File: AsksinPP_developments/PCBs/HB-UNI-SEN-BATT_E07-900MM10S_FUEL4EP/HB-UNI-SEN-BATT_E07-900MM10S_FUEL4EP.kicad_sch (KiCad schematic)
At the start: 32 parts, among them J1 Conn_01x02, J10 charge, J11 ePaper connector, J12 U.FL connector, J2 Conn_01x02, J3 Conn_01x02, J4 Conn_01x02, J5 ISP Programmer, J6 Conn_01x04, J7 Conn_01x04, J8 Conn_01x04, J9 Conn_01x04, Q1 IRLU024N, SW1 config button

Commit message: PCBs: added HB-UNI-SEN-BATT_ATMega1284P_E07-900MM10S_FUEL4EP; fies fixes for HB-UNI-SEN-BATT_ATMega1284P_E07-868MS10_FUEL4EP and HB-UNI-SEN-BATT_E07-900MM10S_FUEL4EP
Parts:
- Module1: footprint U.FL connector (optional) -> FUEL4EP:eByte_E07-900MM10S
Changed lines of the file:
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@@
       (effects (font (size 1.27 1.27) bold))
     )
-    (property "Footprint" "U.FL connector (optional)" (id 2) (at 90.17 181.61 0)
+    (property "Footprint" "FUEL4EP:eByte_E07-900MM10S" (id 2) (at 90.17 181.61 0)
       (effects (font (size 1.27 1.27)) hide)
     )
@@
     )
     (path "/355609ac-841a-4e6b-bbeb-2d1eb180bf65"
-      (reference "Module1") (unit 1) (value "E07-900MM10S") (footprint "U.FL connector (optional)")
+      (reference "Module1") (unit 1) (value "E07-900MM10S") (footprint "FUEL4EP:eByte_E07-900MM10S")
     )
     (path "/00000000-0000-0000-0000-0000615b04ce"

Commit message: PCBs/HB-UNI-SEN-BATT_E07-900MM10S_FUEL4EP: migration to KiCAD 8
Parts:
- removed J12: U.FL connector, FUEL4EP:U.FL_Molex_MCRF_73412-0110_Vertical, symbol Connector:Conn_Coaxial_x2_Isolated
- added J12: U.FL connector, FUEL4EP:U.FL_Molex_MCRF_73412-0110_Vertical, symbol Connector:Conn_Coaxial
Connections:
- net GND: now also J12.2 (Ext)
- net at AE1.1 (A), Module1.1B (ANT): now also J12.1 (In)
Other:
- moved on the sheet: D1, Module2, R1, SW1

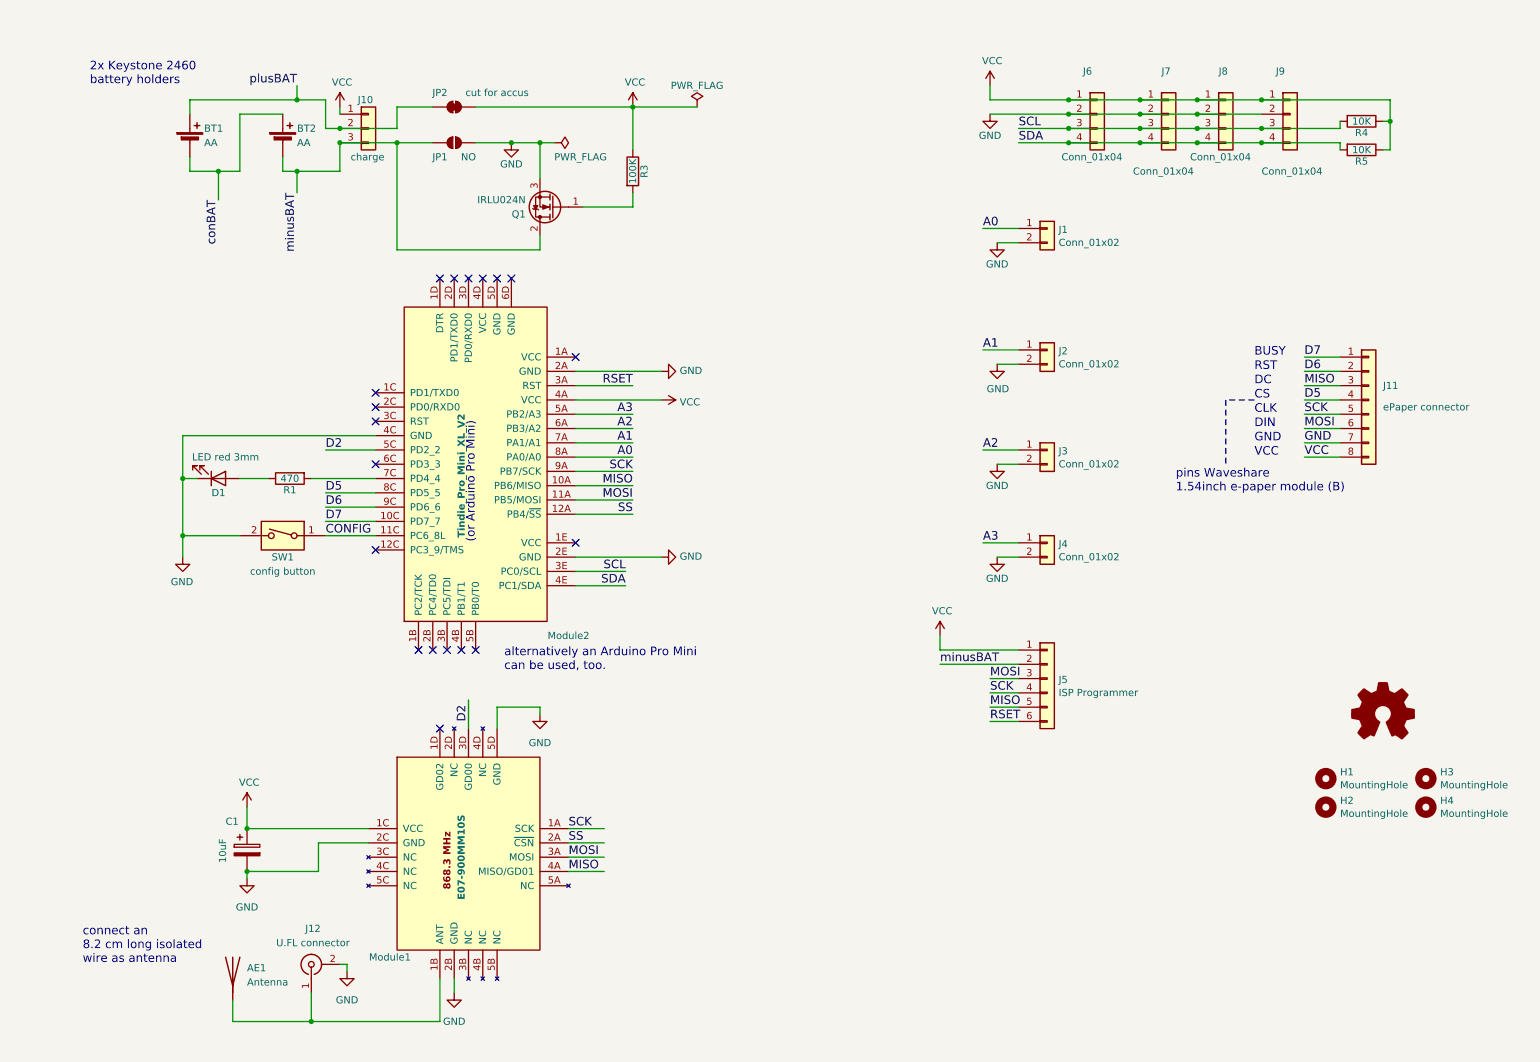
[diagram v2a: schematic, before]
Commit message: update of PCBs/HB-UNI-SEN-BATT_E07-868MS10_FUEL4EP, PCBs/HB-UNI-SEN-BATT_E07-900M10S_FUEL4EP, and PCBs/HB-UNI-SEN-BATT_E07-900MM10S_FUEL4EP to support HB_Pro_Mini_ATMEGA1284P_FUEL4EP
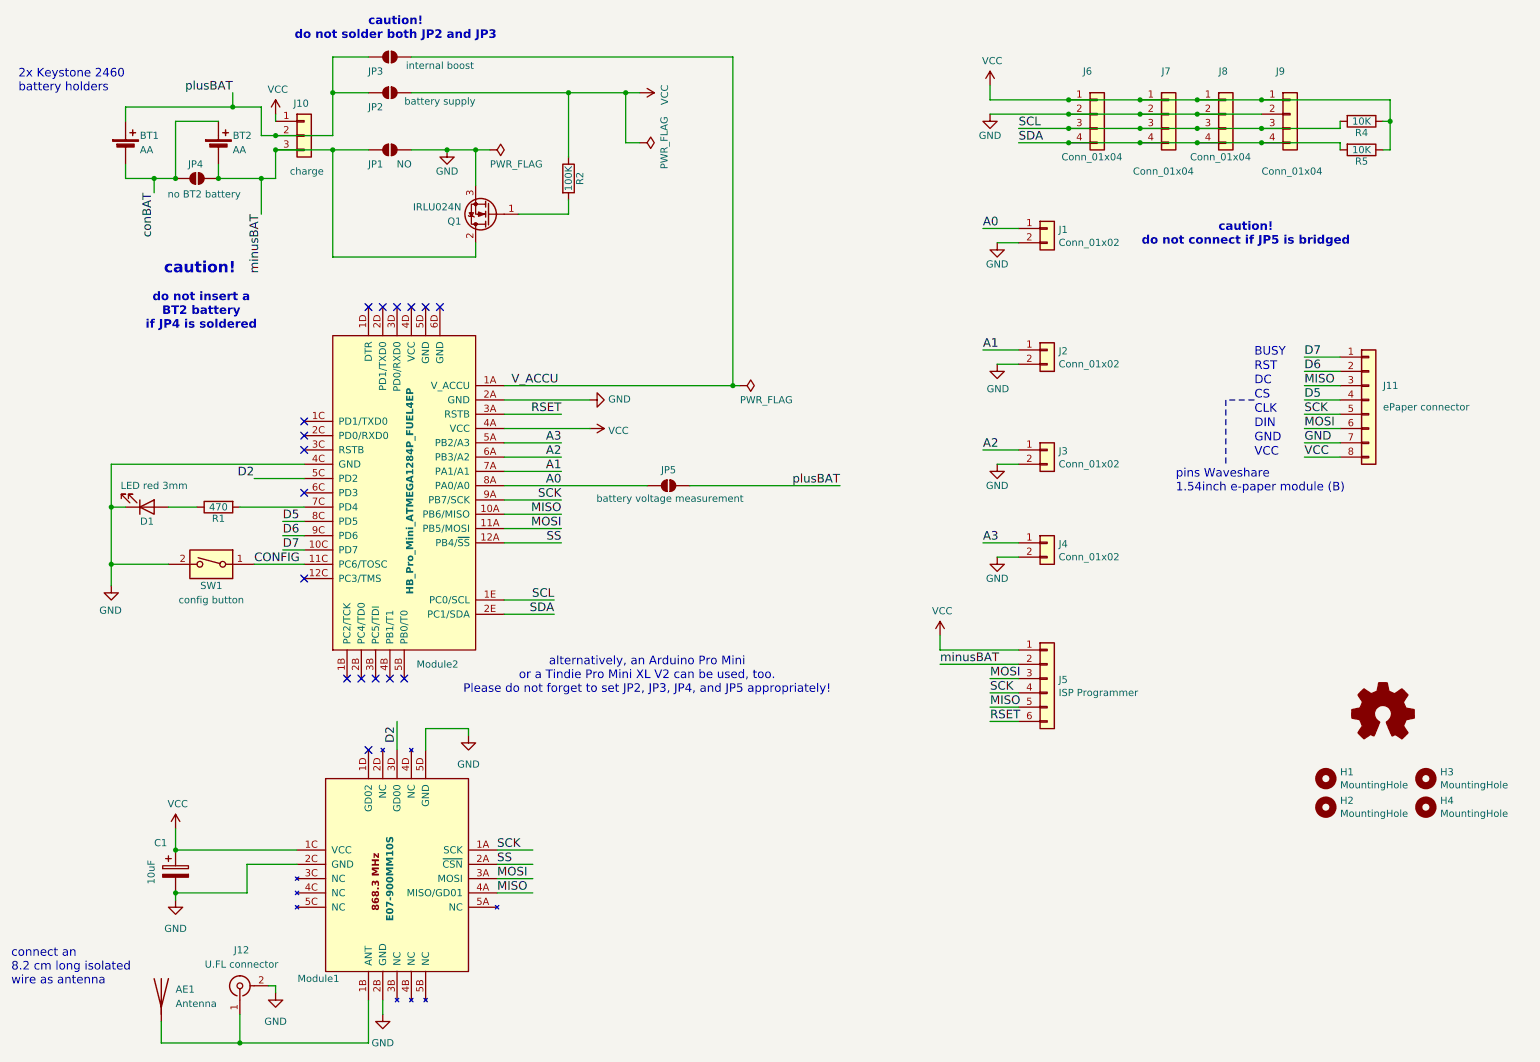
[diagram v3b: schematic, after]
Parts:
- removed JP2: cut for accus, Jumper:SolderJumper-2_P1.3mm_Bridged_Pad1.0x1.5mm, symbol Jumper:SolderJumper_2_Bridged
- removed Module2: Tindie_Pro_Mini_XL_V2, FUEL4EP:Tindie_ArduinoProMiniXL_1284P_V2, symbol FUEL4EP:Tindie_Pro_Mini_XL_V2
- removed R3: 100K, Resistor_THT:R_Axial_DIN0207_L6.3mm_D2.5mm_P2.54mm_Vertical, symbol Device:R
- added JP2: battery supply, Jumper:SolderJumper-2_P1.3mm_Open_Pad1.0x1.5mm, symbol Jumper:SolderJumper_2_Open
- added JP3: internal boost, Jumper:SolderJumper-2_P1.3mm_Open_Pad1.0x1.5mm, symbol Jumper:SolderJumper_2_Open
- added JP4: no BT2 battery, FUEL4EP:SolderJumper-2_P1.3mm_Open_Pad1.0x1.5mm, symbol Jumper:SolderJumper_2_Open
- added JP5: battery voltage measurement, Jumper:SolderJumper-2_P1.3mm_Open_Pad1.0x1.5mm, symbol Jumper:SolderJumper_2_Open
- added Module2: HB_Pro_Mini_ATMEGA1284P_FUEL4EP, FUEL4EP:HB_Pro_Mini_ATMEGA1284P_FUEL4EP, symbol FUEL4EP:HB_Pro_Mini_ATMEGA1284P_FUEL4EP
- added R2: 100K, Resistor_THT:R_Axial_DIN0207_L6.3mm_D2.5mm_P2.54mm_Vertical, symbol Device:R
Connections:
- net A0: now also JP5.1 (A), Module2.8A (PA0/A0)
- net A1: now also Module2.7A (PA1/A1)
- net A2: now also Module2.6A (PB3/A2)
- net A3: now also Module2.5A (PB2/A3)
- net CONFIG: now also Module2.11C (PC6/TOSC)
- net D2: now also Module2.5C (PD2)
- net D5: now also Module2.8C (PD5)
- net D6: now also Module2.9C (PD6)
- net D7: now also Module2.10C (PD7)
- net GND: now also Module2.2A (GND), Module2.4C (GND)
- net MISO: now also Module2.10A (PB6/MISO)
- net MOSI: now also Module2.11A (PB5/MOSI)
- net RSET: now also Module2.3A (RSTB)
- net SCK: now also Module2.9A (PB7/SCK)
- net SCL: now also Module2.1E (PC0/SCL)
- net SDA: now also Module2.2E (PC1/SDA)
- net SS: now also Module2.12A (PB4/~{SS})
- net VCC: now also JP2.2 (B), Module2.4A (VCC), R2.1
- net conBAT: now also JP4.1 (A)
- net minusBAT: now also JP4.2 (B)
- net plusBAT: now also JP2.1 (A), JP3.1 (A), JP5.2 (B)
- net at R1.2: now also Module2.7C (PD4)
- net at Q1.1 (G): now also R2.2
- new net V_ACCU: JP3.2 (B), Module2.1A (V_ACCU)
- no-connect marks 19 -> 17
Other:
- note added: "alternatively, an Arduino Pro Mini or a Tindie Pro Mini XL V2 can be used, too. Please do not forget to set JP2, JP3, JP4, and JP5 appropriately!"
- note added: "caution!"
- note added: "caution! do not connect if JP5 is bridged"
- note added: "caution! do not solder both JP2 and JP3"
- note added: "do not insert a BT2 battery if JP4 is soldered"
- note removed: "(or Arduino Pro Mini)"
- note removed: "alternatively an Arduino Pro Mini can be used, too."
- company: FUEL4EP -> (C) FUEL4EP 2025
- moved on the sheet: AE1, C1, J12, Module1
